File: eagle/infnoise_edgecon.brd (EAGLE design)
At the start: 36.3 x 12.2 mm, 28 parts, among them SW1 MC74VHC1G66DFT1G, SW2 MC74VHC1G66DFT1G, X1 USB

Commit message: update
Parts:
- moved C9 1.47 mm to (32.6, 6.17)
- moved FID3 1.47 mm to (34.1, 11.4)
- moved R7 1.47 mm to (32.6, 9.92)
- moved R8 1.47 mm to (32.6, 2.42)
- moved C1 1.47 mm to (14.6, 1.80)
- moved AMP1 1.47 mm to (30.1, 6.17)
- moved C2 1.47 mm to (18.8, 0.92)
- moved C3 1.47 mm to (18.8, 2.90)
- moved C4 1.47 mm to (12.2, 9.67)
- moved C5 1.47 mm to (12.2, 2.67)
- moved C6 1.47 mm to (16.8, 9.52)
- moved C7 1.47 mm to (21.3, 6.17)
- moved C8 1.47 mm to (23.3, 6.17)
- moved COMP1 1.47 mm to (26.1, 6.17)
- moved L1 1.47 mm to (16.4, 1.80)
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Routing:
- net USB_P: track 10.1 -> 8.63 mm
- net USB_M: track 10.00 -> 8.53 mm
- net VCCIN: track 13.7 -> 12.3 mm
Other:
- board size 36.3 x 12.2 mm -> 34.8 x 12.2 mm

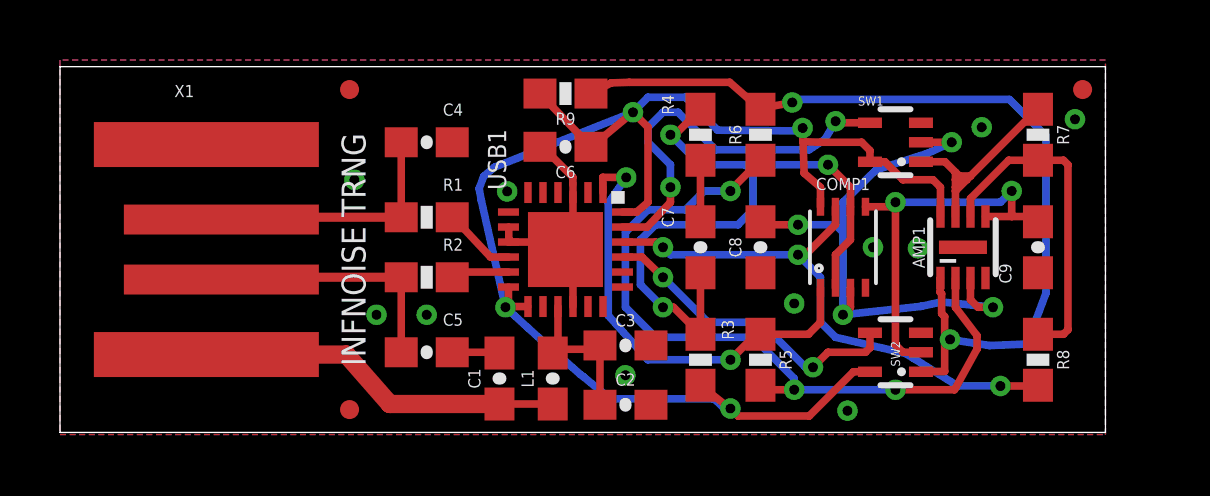
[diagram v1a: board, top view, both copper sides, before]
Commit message: Made 0.5mm pads all the same size and shrank QFN24 center pad
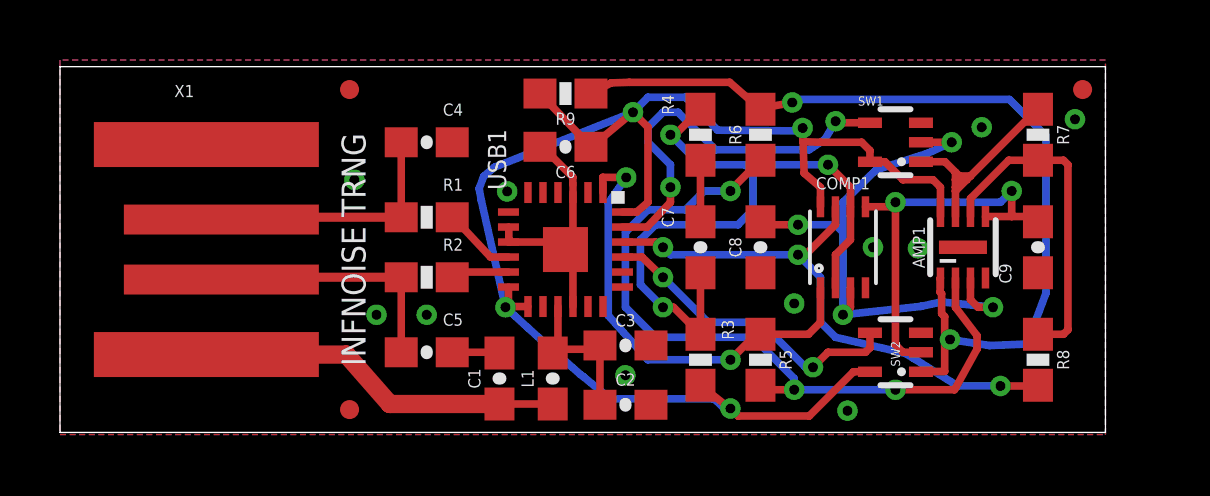
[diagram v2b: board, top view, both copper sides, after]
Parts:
- AMP1: device infnoise:DFN6-2X3 -> infnoise:DFN8-2X3
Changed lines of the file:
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@@
 </autorouter>
 <elements>
-<element name="AMP1" library="infnoise" package="DFN6-2X3" value="TSV912IQ2T" x="30.0988" y="6.1722"/>
+<element name="AMP1" library="infnoise" package="DFN8-2X3" value="TSV912IQ2T" x="30.0988" y="6.1722"/>
 <element name="C8" library="infnoise" package="0603-CAP" value="220pF" x="23.3488" y="6.1722" rot="R90"/>
 <element name="C9" library="infnoise" package="0603-CAP" value="220pF" x="32.5988" y="6.1722" smashed="yes" rot="R90">

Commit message: Changed gain target to 1.84
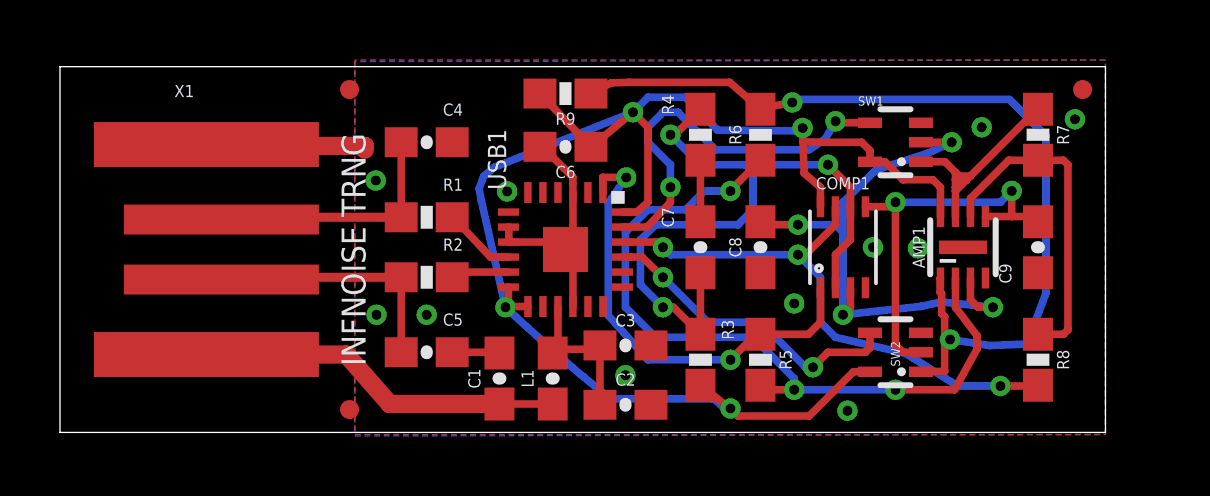
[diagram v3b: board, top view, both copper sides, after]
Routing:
- net GND: track 11.4 -> 13.4 mm
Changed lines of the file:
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@@
 <contactref element="C7" pad="2"/>
 <polygon width="0.254" layer="16">
-<vertex x="0" y="12.4142"/>
-<vertex x="0" y="-0.0698"/>
+<vertex x="9.8298" y="12.3634"/>
+<vertex x="9.8298" y="-0.1206"/>
 <vertex x="34.8488" y="-0.0698"/>
 <vertex x="34.8488" y="12.4142"/>
 </polygon>
 <polygon width="0.254" layer="1">
-<vertex x="0" y="12.4142"/>
-<vertex x="0" y="-0.0698"/>
+<vertex x="9.8298" y="12.4142"/>
+<vertex x="9.8298" y="-0.0698"/>
 <vertex x="34.8488" y="-0.0698"/>
 <vertex x="34.8488" y="12.4142"/>
@@
 <wire x1="17.0988" y1="5.9222" x2="16.8488" y2="6.096" width="0.254" layer="1"/>
 <via x="10.5506" y="3.9222" extent="1-16" drill="0.3302"/>
-<via x="9.814" y="8.4222" extent="1-16" drill="0.3302"/>
+<via x="10.5252" y="8.3968" extent="1-16" drill="0.3302"/>
 <wire x1="17.0988" y1="7.996" x2="17.0988" y2="6.4222" width="0.254" layer="1"/>
 <wire x1="17.0988" y1="6.4222" x2="16.8488" y2="6.096" width="0.254" layer="1"/>
@@
 <wire x1="17.0942" y1="8.255" x2="17.0942" y2="8.509" width="0.254" layer="1"/>
 <wire x1="17.0942" y1="8.509" x2="16.4084" y2="9.1948" width="0.254" layer="1"/>
+<wire x1="8.255" y1="9.5504" x2="10.16" y2="9.5504" width="0.6096" layer="1"/>
+<wire x1="10.16" y1="9.5504" x2="10.16" y2="9.4234" width="0.6096" layer="1"/>
 <wire x1="17.0988" y1="7.996" x2="17.0942" y2="8.255" width="0" layer="19" extent="1-1"/>
+<wire x1="4.88" y1="9.596" x2="8.255" y2="9.5504" width="0" layer="19" extent="1-1"/>
 </signal>
 <signal name="VCC33">
